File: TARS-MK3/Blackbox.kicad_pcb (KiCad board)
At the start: 2 copper layers, 48.3 x 20.3 mm, 0 parts

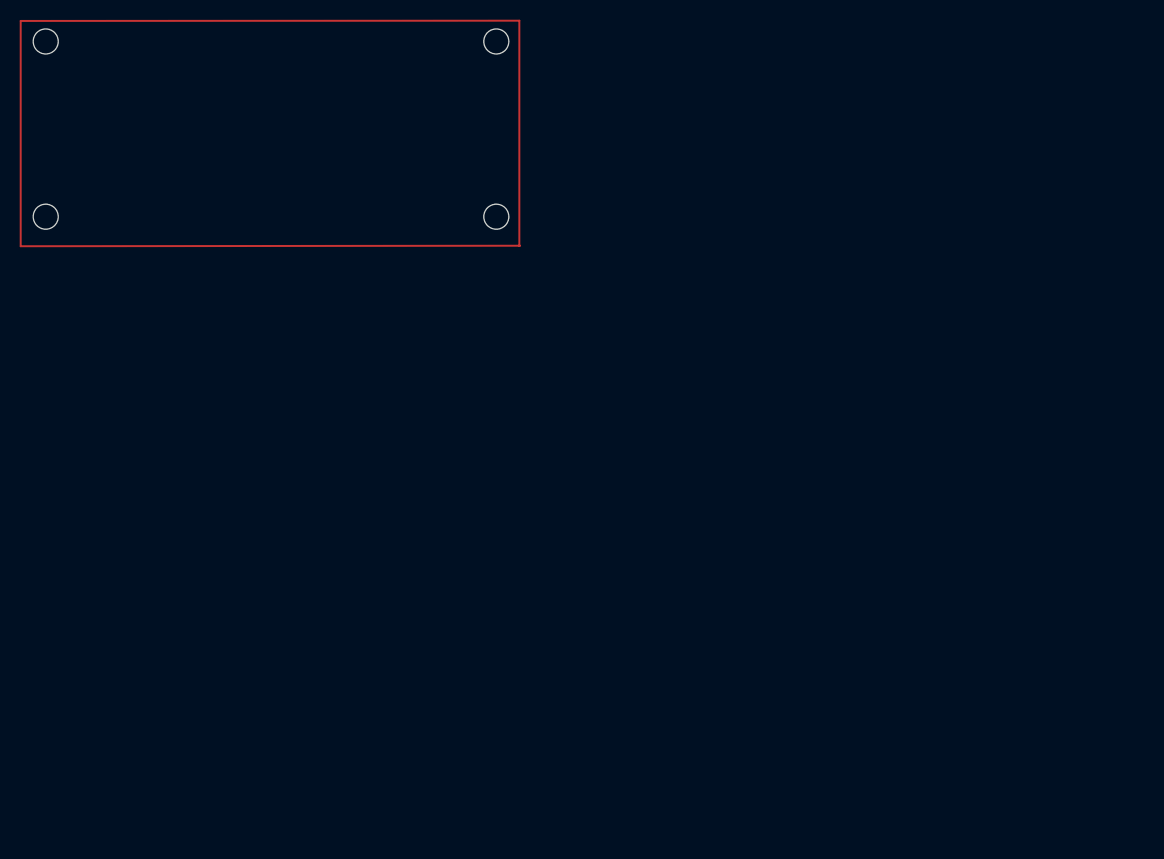
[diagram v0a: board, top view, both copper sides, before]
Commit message: placed things on blackbox
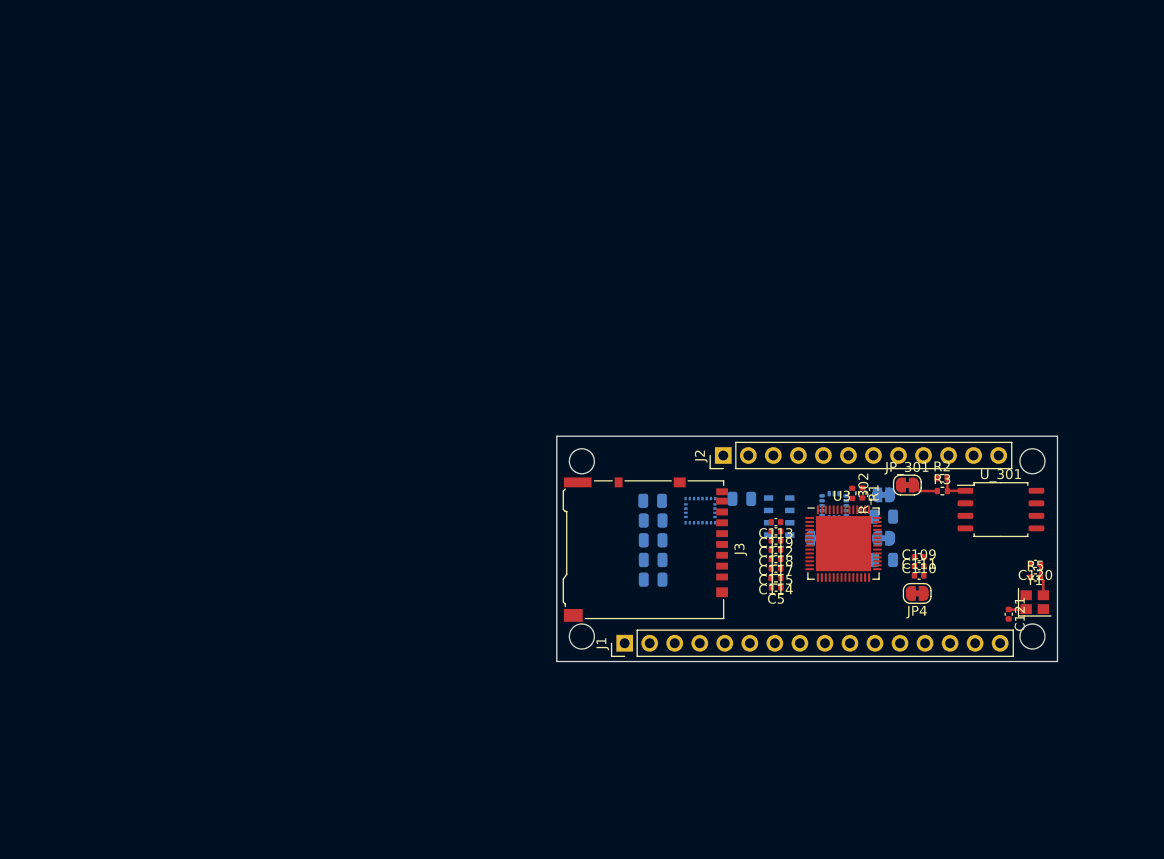
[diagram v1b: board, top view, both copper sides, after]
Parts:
- added C101: 100nF, Capacitor_SMD:C_0805_2012Metric, B.Cu at (150.2, 107.6)
- added C102: 10uF, Capacitor_SMD:C_0805_2012Metric, B.Cu at (173.6, 103.2)
- added C103: 0.1uF, Capacitor_SMD:C_0805_2012Metric, B.Cu at (173.6, 107.6)
- added C104: 100 nF, Capacitor_SMD:C_0805_2012Metric, B.Cu at (150.2, 103.6)
- added C105: 100 nF, Capacitor_SMD:C_0805_2012Metric, B.Cu at (150.2, 101.6)
- added C106: 10 uF, Capacitor_SMD:C_0805_2012Metric, B.Cu at (150.2, 105.6)
- added C107: 10 nF, Capacitor_SMD:C_0805_2012Metric, B.Cu at (159.2, 101.4)
- added C108: 100 nF, Capacitor_SMD:C_0805_2012Metric, B.Cu at (150.2, 109.6)
- added C109: 100n, Capacitor_SMD:C_0402_1005Metric, F.Cu at (177.2, 108.2)
- added C110: 100n, Capacitor_SMD:C_0402_1005Metric, F.Cu at (177.2, 107.3)
- added C111: 1u, Capacitor_SMD:C_0402_1005Metric, F.Cu at (177.2, 109.2)
- added C112: 1u, Capacitor_SMD:C_0402_1005Metric, F.Cu at (162.7, 105.6)
- added C113: 100n, Capacitor_SMD:C_0402_1005Metric, F.Cu at (162.7, 103.8)
- added C114: 100n, Resistor_SMD:R_0402_1005Metric, F.Cu at (162.7, 109.4)
- added C115: 100n, Capacitor_SMD:C_0402_1005Metric, F.Cu at (162.7, 108.5)
- added C116: 100n, Resistor_SMD:R_0402_1005Metric, B.Cu at (170.2, 106.4)
- added C117: 100n, Capacitor_SMD:C_0402_1005Metric, F.Cu at (162.7, 107.5)
- added C118: 100n, Capacitor_SMD:C_0402_1005Metric, F.Cu at (162.7, 106.6)
- added C119: 100n, Capacitor_SMD:C_0402_1005Metric, F.Cu at (162.7, 104.7)
- added C120: LOAD_C, Capacitor_SMD:C_0402_1005Metric, F.Cu at (189.0, 108.0)
- added C121: LOAD_C, Capacitor_SMD:C_0402_1005Metric, F.Cu at (186.3, 113.1)
- added C122: 100 nF, Capacitor_SMD:C_0402_1005Metric, B.Cu at (170.2, 108.4)
- added C5: 100n, Capacitor_SMD:C_0402_1005Metric, F.Cu at (162.7, 110.4)
- added J1: RP Header 16 pin, Connector_PinHeader_2.54mm:PinHeader_1x16_P2.54mm_Vertical, F.Cu at (147.3, 116.1)
- added J2: RP Header 12 pin, Connector_PinHeader_2.54mm:PinHeader_1x12_P2.54mm_Vertical, F.Cu at (157.3, 97.0)
- added J3: Micro_SD_Card, Connector_Card:microSD_HC_Hirose_DM3AT-SF-PEJM5, F.Cu at (149.5, 106.6)
- added JP1: Jumper_NC_Small, Jumper:SolderJumper-2_P1.3mm_Bridged_RoundedPad1.0x1.5mm, B.Cu at (166.8, 105.4)
- added JP2: Jumper_NC_Small, Jumper:SolderJumper-2_P1.3mm_Bridged_RoundedPad1.0x1.5mm, B.Cu at (173.6, 101.0)
- added JP3: Jumper_NC_Small, Jumper:SolderJumper-2_P1.3mm_Bridged_RoundedPad1.0x1.5mm, B.Cu at (173.6, 105.4)
- added JP4: Jumper, Jumper:SolderJumper-2_P1.3mm_Bridged_RoundedPad1.0x1.5mm, F.Cu at (177.0, 111.0)
- added JP_301: Jumper, Jumper:SolderJumper-2_P1.3mm_Bridged_RoundedPad1.0x1.5mm, F.Cu at (176.0, 100.0)
- added R1: 27.4, Resistor_SMD:R_0402_1005Metric, F.Cu at (171.4, 100.8)
- added R101: 16k, Resistor_SMD:R_0402_1005Metric, B.Cu at (170.2, 107.4)
- added R102: 16k, Resistor_SMD:R_0402_1005Metric, B.Cu at (170.2, 105.4)
- added R2: DNF, Resistor_SMD:R_0402_1005Metric, F.Cu at (179.5, 99.3)
- added R3: R, Resistor_SMD:R_0402_1005Metric, F.Cu at (179.6, 100.6)
- added R5: 1k, Capacitor_SMD:C_0402_1005Metric, F.Cu at (189.0, 109.4)
- added R_302: 27.4, Resistor_SMD:R_0402_1005Metric, F.Cu at (170.4, 100.8)
- added U1: H3LIS331DL, Package_LGA:LGA-16_3x3mm_P0.5mm_LayoutBorder3x5y, B.Cu at (168.6, 102.1)
- added U2: LSM9DS1, Package_LGA:LGA-24L_3x3.5mm_P0.43mm, B.Cu at (155.0, 102.6)
- added U3: RP2040_chip, Package_DFN_QFN:QFN-56-1EP_7x7mm_P0.4mm_EP5.6x5.6mm, F.Cu at (169.5, 105.9)
- added U4: MS5611-01BA, Package_LGA:LGA-8_3x5mm_P1.25mm, B.Cu at (163.0, 103.2)
- added U_301: W25Q128JVS, Package_SO:SOIC-8_5.23x5.23mm_P1.27mm, F.Cu at (185.5, 102.5)
- added Y1: Crystal_GND24, Crystal:Crystal_SMD_2520-4Pin_2.5x2.0mm, F.Cu at (188.9, 111.9)
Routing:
- net Net-(R2-Pad2): track 0.00 -> 3.33 mm
- net Net-(C120-Pad1): track 0.00 -> 3.32 mm
- net Net-(R3-Pad1): track 0.00 -> 2.78 mm
- net Net-(C121-Pad1): track 0.00 -> 1.90 mm
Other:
- board size 48.3 x 20.3 mm -> 50.8 x 22.9 mm

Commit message: Changes to BlackBox Schematic, PCB
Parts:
- moved C120 28.0 mm to (161.0, 106.5), turned to 90 degrees
- moved Y1 25.8 mm to (163.8, 106.2), turned to 180 degrees
- moved C115 24.5 mm to (149.2, 129.0)
- moved C114 24.4 mm to (165.0, 133.8)
- moved C5 24.2 mm to (155.0, 133.3)
- moved C110 22.5 mm to (195.0, 121.1), turned to 0 degrees
- moved C121 21.1 mm to (166.8, 105.0), turned to 90 degrees
- moved C111 20.5 mm to (188.2, 126.5)
- moved C117 20.5 mm to (164.0, 128.0)
- moved C118 20.3 mm to (154.2, 125.0)
- moved C119 19.4 mm to (151.5, 120.5)
- moved C113 19.0 mm to (162.2, 122.8)
- moved JP4 18.3 mm to (172.8, 128.8)
- moved C112 16.1 mm to (178.5, 108.8), turned to 0 degrees
- moved R5 12.7 mm to (198.8, 117.5)
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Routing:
- net Net-(R2-Pad2): track 3.33 -> 0.00 mm
- net Net-(C120-Pad1): track 3.32 -> 0.00 mm
- net Net-(R3-Pad1): track 2.78 -> 0.00 mm
- net Net-(C121-Pad1): track 1.90 -> 0.00 mm

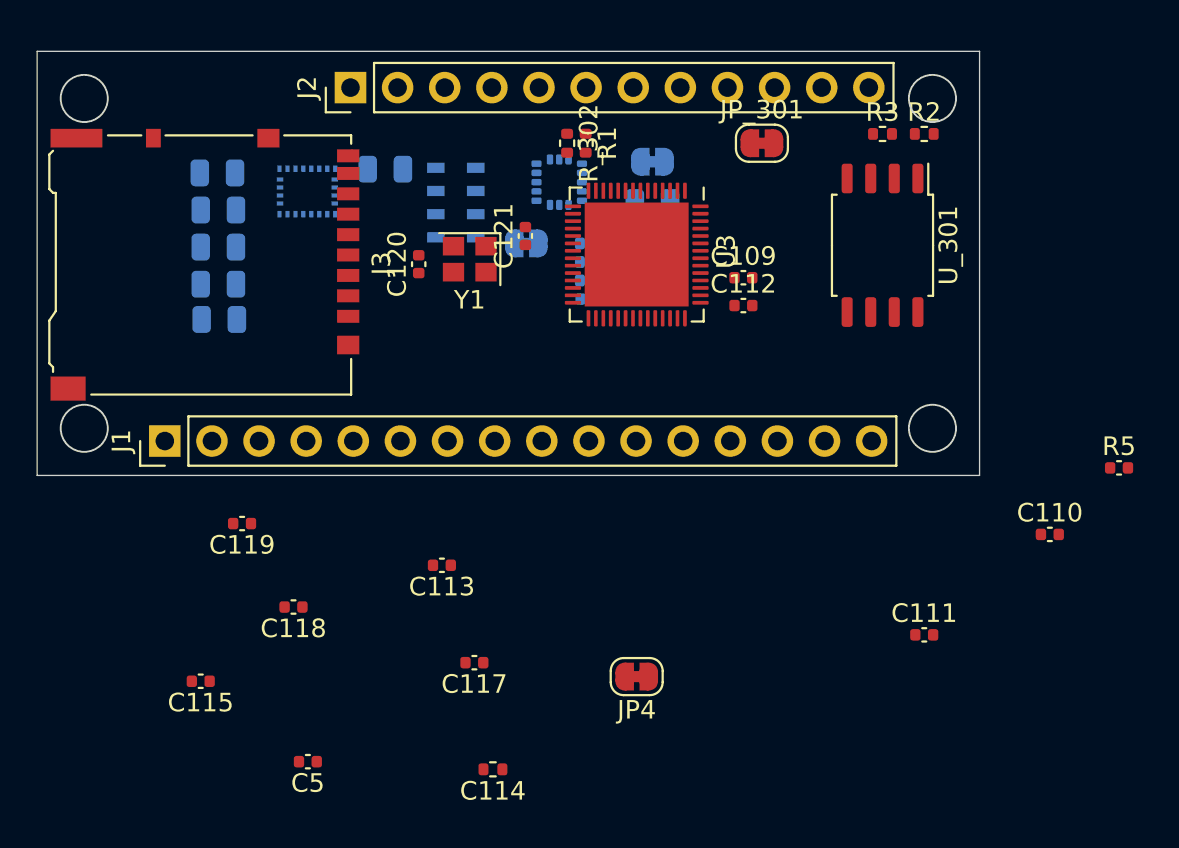
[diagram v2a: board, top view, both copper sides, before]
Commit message: Tracing for Blackbox
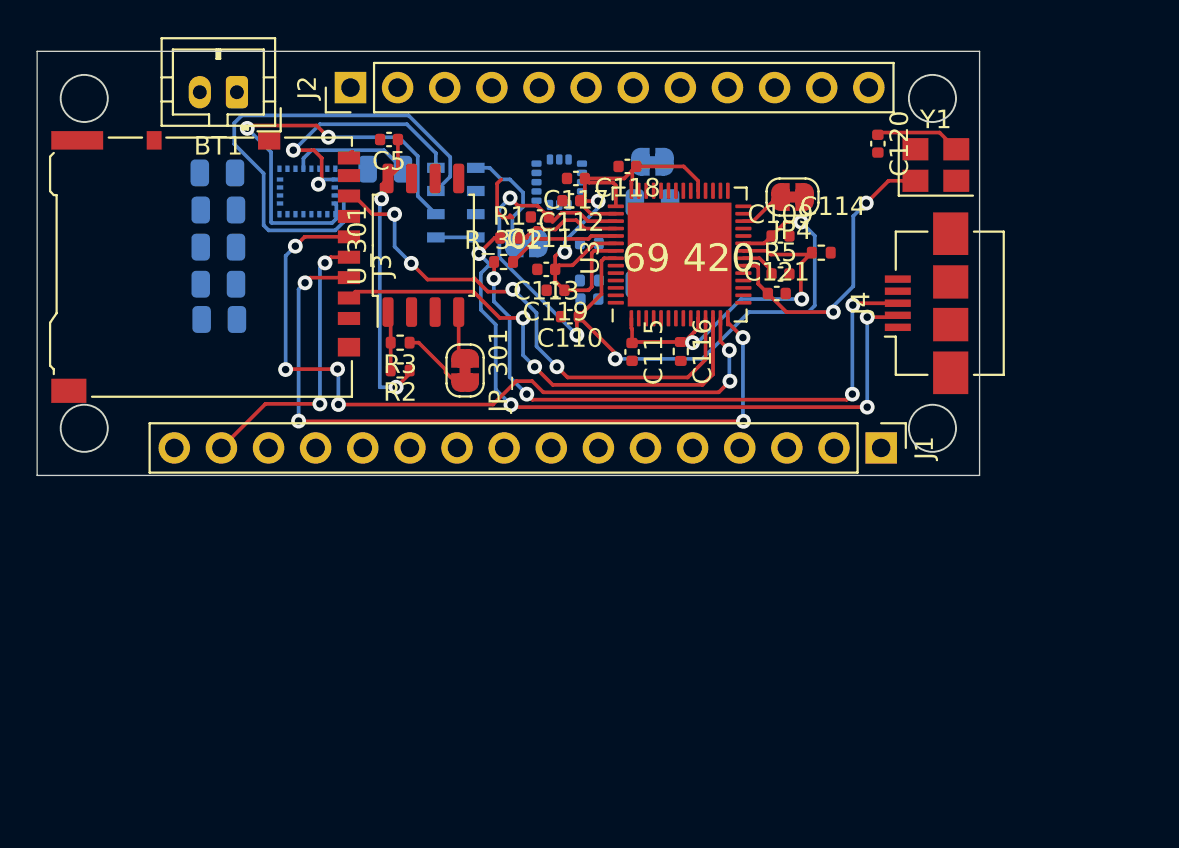
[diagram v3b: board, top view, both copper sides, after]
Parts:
- added BT1: LiPo, Connector_JST:JST_PH_B2B-PH-K_1x02_P2.00mm_Vertical, F.Cu at (151.2, 97.2)
- added J4: USB_B_Micro, Connector_USB:USB_Micro-B_Amphenol_10104110_Horizontal, F.Cu at (188.4, 108.6)
- C116: moved to F.Cu
- Y1: footprint Crystal:Crystal_SMD_2520-4Pin_2.5x2.0mm -> Crystal:Crystal_SMD_3225-4Pin_3.2x2.5mm
- moved J1 38.6 mm to (185.9, 116.4), turned to -90 degrees
- moved C5 33.8 mm to (159.4, 99.8)
- moved C114 33.0 mm to (182.7, 105.9), turned to 0 degrees
- moved R2 31.0 mm to (160.0, 112.2), turned to 180 degrees
- moved C111 30.6 mm to (167.5, 104.0), turned to 180 degrees
- moved C118 29.8 mm to (172.2, 101.2)
- moved C115 29.3 mm to (172.5, 111.2), turned to -90 degrees
- moved C110 28.4 mm to (169.2, 109.3), turned to 180 degrees
- moved R3 28.3 mm to (160.0, 110.8), turned to 180 degrees
- moved JP4 27.2 mm to (181.2, 102.9)
- moved C117 26.7 mm to (169.5, 101.9)
- moved Y1 25.6 mm to (188.9, 101.2), turned to 0 degrees
- moved C120 25.6 mm to (185.8, 100.0), turned to -90 degrees
- moved U_301 24.8 mm to (161.2, 105.5), turned to 90 degrees
- moved C119 21.1 mm to (168.4, 107.9)
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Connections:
- J1 pad 4: /SPIO_MISO -> /SNS_SPI_MISO
- J1 pad 5: /SPIO_MOSI -> /SNS_SPI_MOSI
- J1 pad 6: /SPIO_SCK -> /SNS_SPI_SCK
- U3 pad 11: /SPI1_MISO -> /SPI_SDCARD_MISO
- U3 pad 12: /SPI1_CSn -> /SPI_SDCARD_CS
- U3 pad 13: /SP1_SCK -> /SPI_SDCARD_SCK
- U3 pad 14: /SP1_MOSI -> /SPI_SDCARD_MOSI
- U3 pad 2: /SPI0_MISO -> /SNS_SPI_MISO
- U3 pad 3: /SPI0_CSn -> /MS5611_CS
- U3 pad 4: /SPI0_SCK -> /SNS_SPI_SCK
- U3 pad 5: /SPI0_MOSI -> /SNS_SPI_MOSI
- U3 pad 6: unconnected-(U3-Pad6) -> /LSM9_CS_M
- U3 pad 9: unconnected-(U3-Pad9) -> /H3LIS331DL_CS
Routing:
- net +3V3: track 0.00 -> 66.7 mm, vias 0 -> 6
- net +1V1: track 0.00 -> 44.7 mm, vias 0 -> 4
- net /SPI_SDCARD_SCK: track 0.00 -> 40.4 mm, vias 0 -> 6
- net /SPI_SDCARD_MOSI: track 0.00 -> 40.0 mm, vias 0 -> 4
- net /USB_D-: track 0.00 -> 36.7 mm, vias 0 -> 4
- net /USB_D+: track 0.00 -> 32.9 mm, vias 0 -> 4
- net /SPI_SDCARD_MISO: track 0.00 -> 28.1 mm, vias 0 -> 4
- net /SNS_SPI_MOSI: track 0.00 -> 27.6 mm
- net /SPI_SDCARD_CS: track 0.00 -> 26.8 mm, vias 0 -> 2
- net /SNS_SPI_MISO: track 0.00 -> 24.1 mm, vias 0 -> 2
- net Net-(C121-Pad1): track 0.00 -> 16.3 mm, vias 0 -> 2
- net /3V3: track 0.00 -> 15.4 mm, vias 0 -> 2
- net /SNS_SPI_SCK: track 0.00 -> 13.9 mm, vias 0 -> 2
- net Net-(C101-Pad2): track 0.00 -> 9.09 mm
- net Net-(C107-Pad1): track 0.00 -> 6.53 mm
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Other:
- board text added: "69 420"

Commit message: blackbox PCB changes
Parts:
- moved C103 33.2 mm to (145.8, 89.5)
- moved C102 28.9 mm to (144.8, 104.4), turned to -90 degrees
- moved C122 27.2 mm to (150.9, 89.2)
- moved JP1 25.0 mm to (172.1, 81.0)
- moved R101 23.0 mm to (156.0, 89.3)
- moved JP3 22.2 mm to (152.1, 99.9)
- moved R102 18.4 mm to (161.0, 89.4)
- moved C108 15.1 mm to (135.5, 112.9)
- moved C101 14.8 mm to (135.4, 108.1)
- moved JP2 12.6 mm to (167.4, 90.0)
- moved C107 12.3 mm to (146.9, 100.6), turned to 90 degrees
- moved U2 7.09 mm to (148.1, 104.4)
- moved U1 6.26 mm to (174.5, 100.1)
- moved C106 5.12 mm to (149.3, 100.6), turned to 90 degrees
- moved U4 3.89 mm to (165.3, 100.1), turned to -90 degrees
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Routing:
- net /LSM9_CS_M: track 0.00 -> 33.9 mm, vias 0 -> 5
- net /SNS_SPI_SCK: track 13.9 -> 0.00 mm, vias 2 -> 0
- net Net-(C104-Pad1): track 0.07 -> 10.6 mm
- net /SNS_SPI_MISO: track 24.1 -> 33.6 mm
- net /SNS_SPI_MOSI: track 27.6 -> 19.6 mm, vias 0 -> 2
- net Net-(C101-Pad2): track 9.09 -> 2.97 mm
- net Net-(C107-Pad1): track 6.53 -> 2.05 mm
- net +1V1: track 44.7 -> 48.1 mm
- net /MS5611_CS: track 2.15 -> 0.00 mm
- net +3V3: track 66.7 -> 67.5 mm

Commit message: BlackBox PCB updates
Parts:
- moved U1 5.08 mm to (179.6, 100.1), turned to 90 degrees
- moved JP_301 1.37 mm to (162.6, 111.3), turned to 180 degrees
- moved C110 1.21 mm to (170.2, 108.7)
- moved C118 1.06 mm to (173.2, 100.8)
- moved C111 0.88 mm to (168.4, 103.9)
- moved C116 0.82 mm to (175.8, 111.0)
- moved C5 0.78 mm to (159.4, 100.6)
- moved C120 0.69 mm to (186.4, 100.0)
- moved C114 0.58 mm to (182.1, 105.9)
- moved C121 0.33 mm to (180.6, 108.0)
- moved C112 0.30 mm to (169.4, 102.9)
- moved C115 0.26 mm to (172.5, 111.3)
- moved R5 0.15 mm to (180.6, 106.9)
- moved C117 0.07 mm to (169.4, 101.9)
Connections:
- U3 pad 2: /SNS_SPI_MISO -> unconnected-(U3-Pad2)
- U3 pad 27: unconnected-(U3-Pad27) -> /MS5611_CS
- U3 pad 28: unconnected-(U3-Pad28) -> /SNS_SPI_SCK
- U3 pad 29: unconnected-(U3-Pad29) -> /SNS_SPI_MISO
- U3 pad 3: /MS5611_CS -> unconnected-(U3-Pad3)
- U3 pad 31: unconnected-(U3-Pad31) -> /SNS_SPI_MOSI
- U3 pad 32: unconnected-(U3-Pad32) -> /H3LIS331DL_CS
- U3 pad 36: unconnected-(U3-Pad36) -> /MS5611_CS
- U3 pad 4: /SNS_SPI_SCK -> unconnected-(U3-Pad4)
- U3 pad 5: /SNS_SPI_MOSI -> unconnected-(U3-Pad5)
- U3 pad 9: /H3LIS331DL_CS -> unconnected-(U3-Pad9)
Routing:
- net /SNS_SPI_SCK: track 0.00 -> 46.7 mm, vias 0 -> 5
- net /SNS_SPI_MOSI: track 19.6 -> 38.1 mm, vias 2 -> 4
- net Net-(C120-Pad1): track 4.65 -> 16.8 mm, vias 0 -> 2
- net /MS5611_CS: track 0.00 -> 11.4 mm, vias 0 -> 3
- net /SNS_SPI_MISO: track 33.6 -> 40.9 mm, vias 2 -> 4
- net +3V3: track 67.5 -> 74.6 mm, vias 6 -> 10
- net /SPI_SDCARD_SCK: track 40.4 -> 46.1 mm
- net /H3LIS331DL_CS: track 0.00 -> 5.51 mm, vias 0 -> 1
- net /SPI_SDCARD_MOSI: track 40.0 -> 45.3 mm
- net /SPI_SDCARD_MISO: track 28.1 -> 32.3 mm
- net /LSM9_CS_M: track 33.9 -> 37.8 mm, vias 5 -> 3
- net Net-(C101-Pad2): track 2.97 -> 0.00 mm
- net /SPI_SDCARD_CS: track 26.8 -> 29.4 mm
- net /USB_D-: track 36.7 -> 39.2 mm
- net Net-(JP_301-Pad2): track 3.11 -> 1.61 mm
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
